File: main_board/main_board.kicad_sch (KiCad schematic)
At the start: 102 parts, among them J1 3.5mm Jack, J18 Conn_01x15_Female, J19 Conn_01x15_Female, J2 3.5mm Jack, J20 Conn_01x02_Male, J21 OLED Pins, J3 3.5mm Jack, J4 3.5mm Jack, J5 Display Header, J6 EU Power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

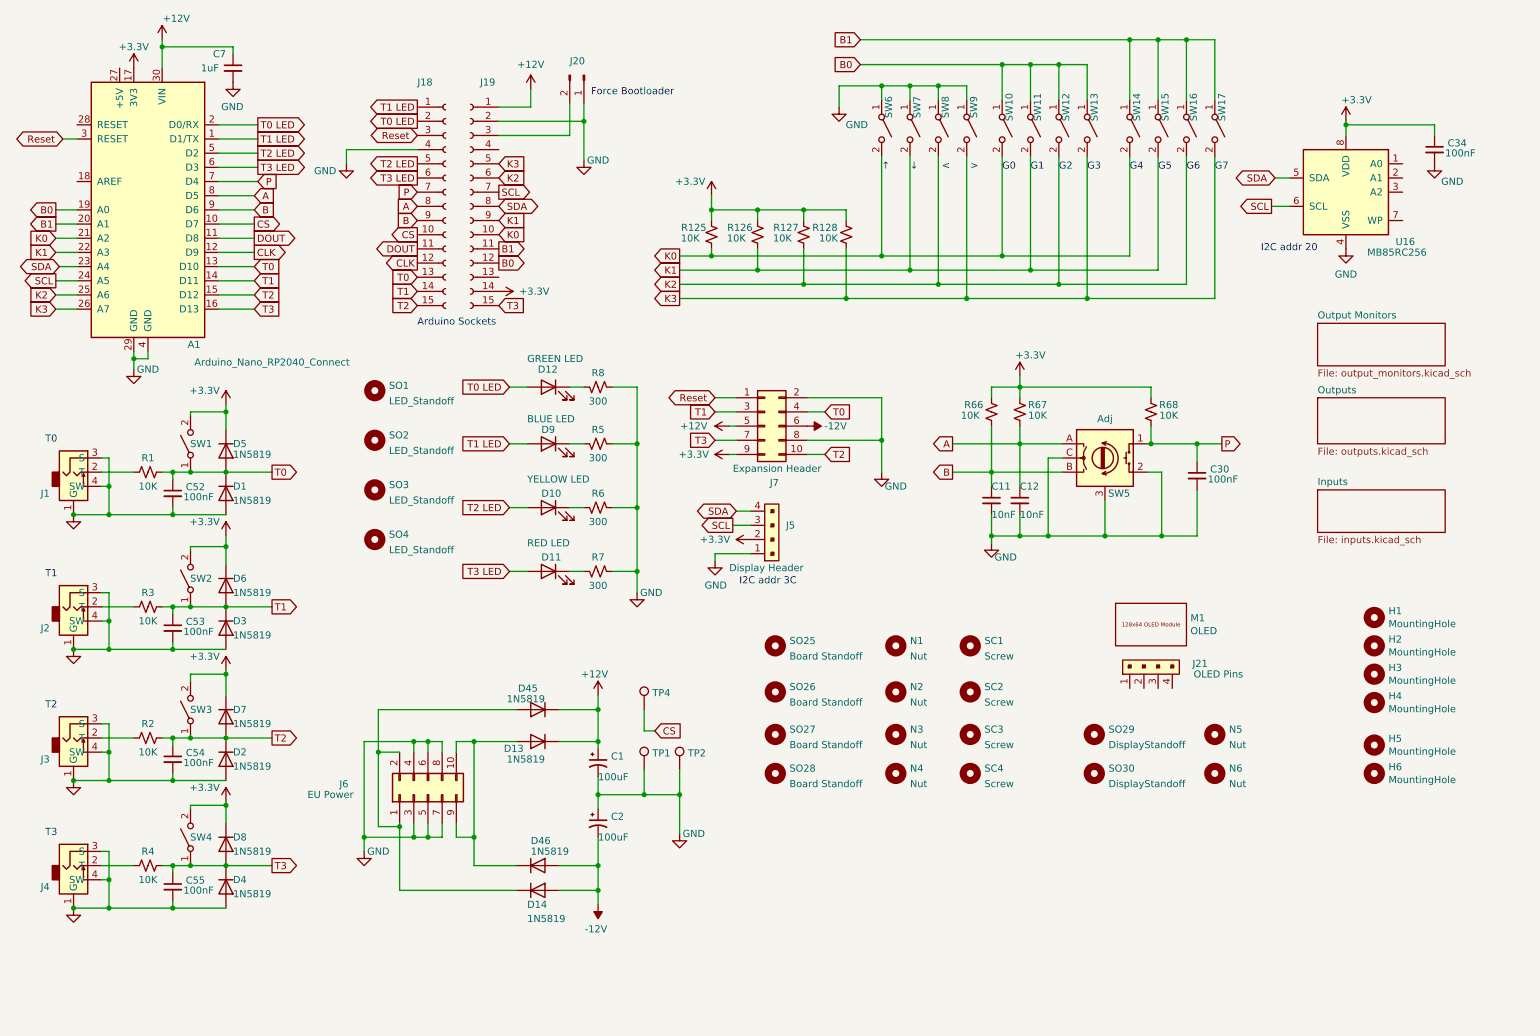
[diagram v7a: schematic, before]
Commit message: New layout. Fixes regulator chip pinout error.
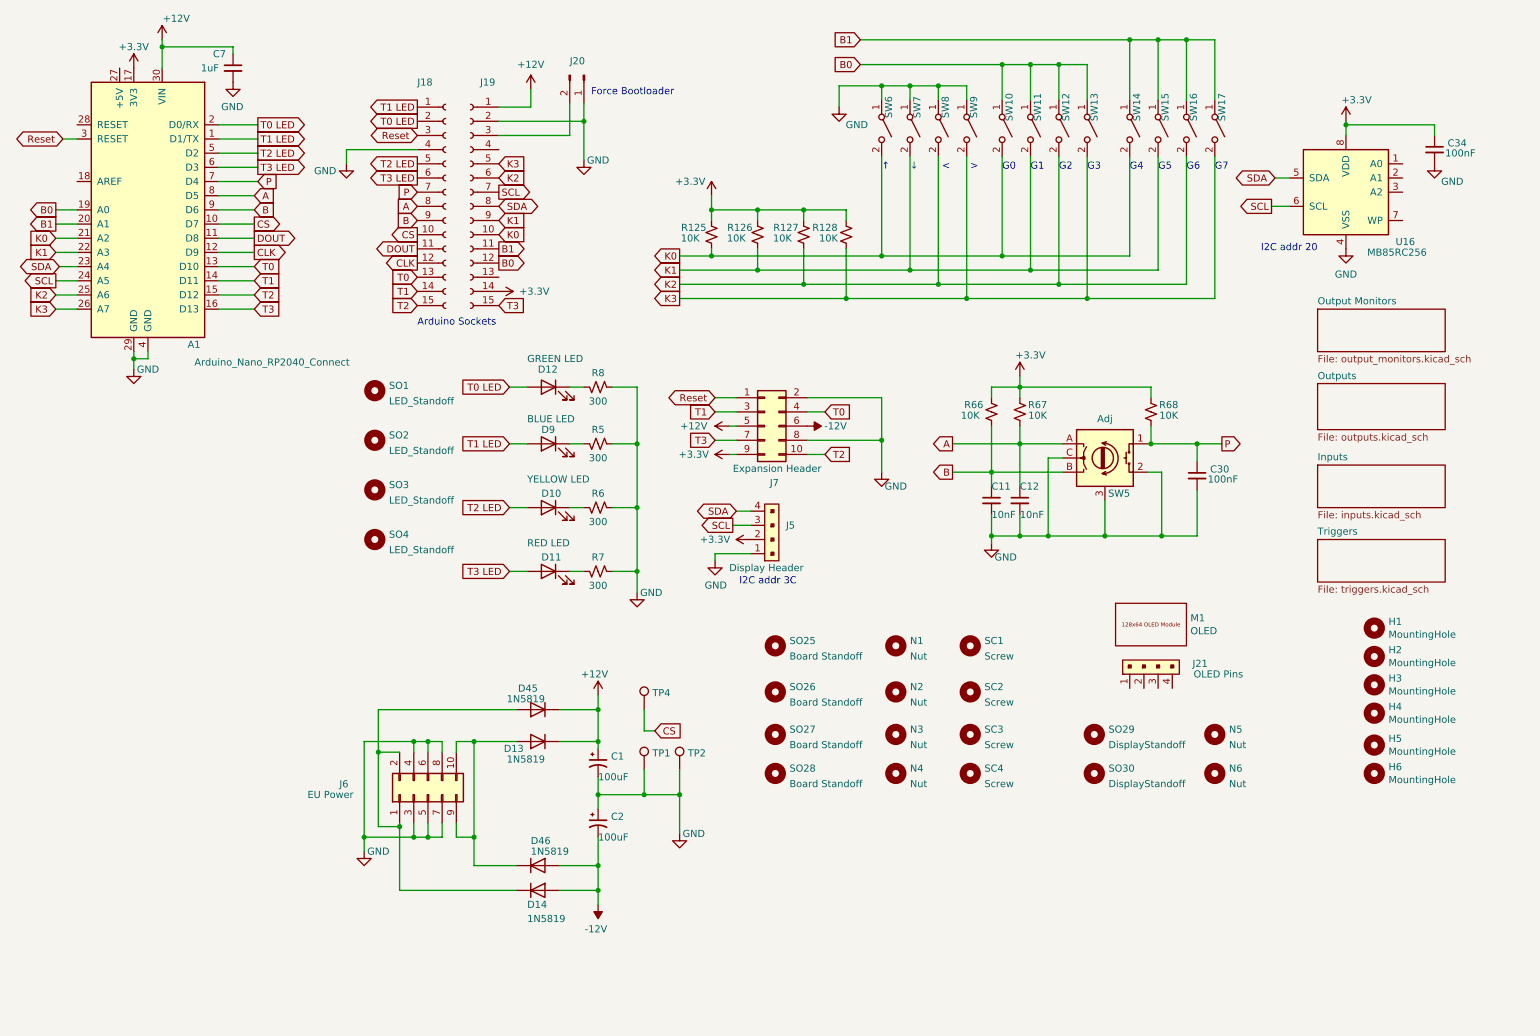
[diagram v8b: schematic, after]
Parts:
- removed C52, C53, C54, C55: 100nF, Capacitor_SMD:C_0805_2012Metric_Pad1.18x1.45mm_HandSolder, symbol Device:C_Small
- removed D1, D2, D3, D4, D5, D6, D7, D8: 1N5819, Diode_SMD:D_0805_2012Metric_Pad1.15x1.40mm_HandSolder, symbol Diode:1N4148
- removed J1, J2, J3, J4: 3.5mm Jack, sputterizer:Molex-0472570001, symbol greenface-symbols:Molex_47257
- removed R1, R2, R3, R4: 10K, Resistor_SMD:R_0805_2012Metric_Pad1.20x1.40mm_HandSolder, symbol Device:R_Small_US
- removed SW1, SW2, SW3, SW4: Push Button, Button_Switch_THT:SW_PUSH_6mm, symbol Switch:SW_SPST
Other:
- added sheet Triggers (triggers.kicad_sch)
- note removed: "T0"
- note removed: "T1"
- note removed: "T2"
- note removed: "T3"
- moved on the sheet: H1, H2, H3, H4
